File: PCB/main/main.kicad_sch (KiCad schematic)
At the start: 4 parts, among them J1 Conn_01x33_Female, J2 Conn_01x33_Female, J3 Conn_01x33_Female, J4 Conn_01x33_Female

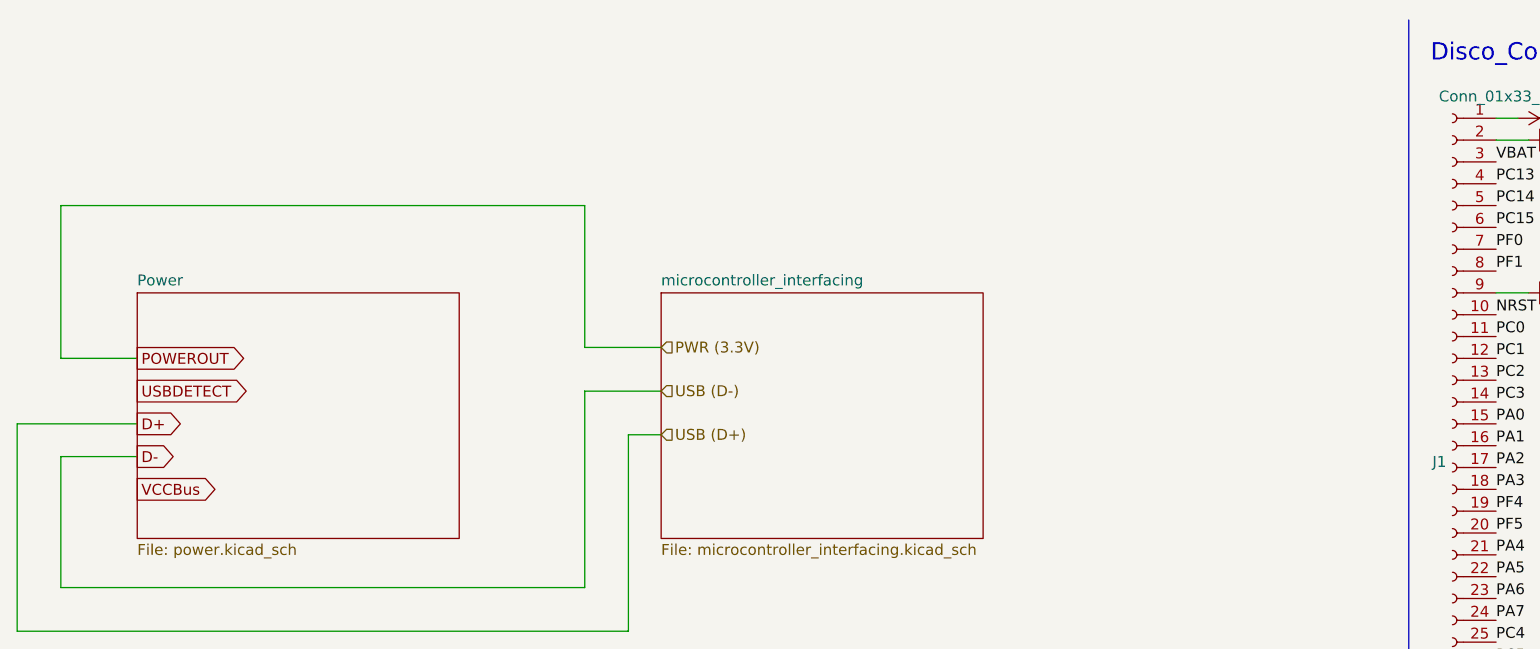
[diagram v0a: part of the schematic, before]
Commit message: Power v0.1, Sensing v0.1, uC Control v0.1, ERC
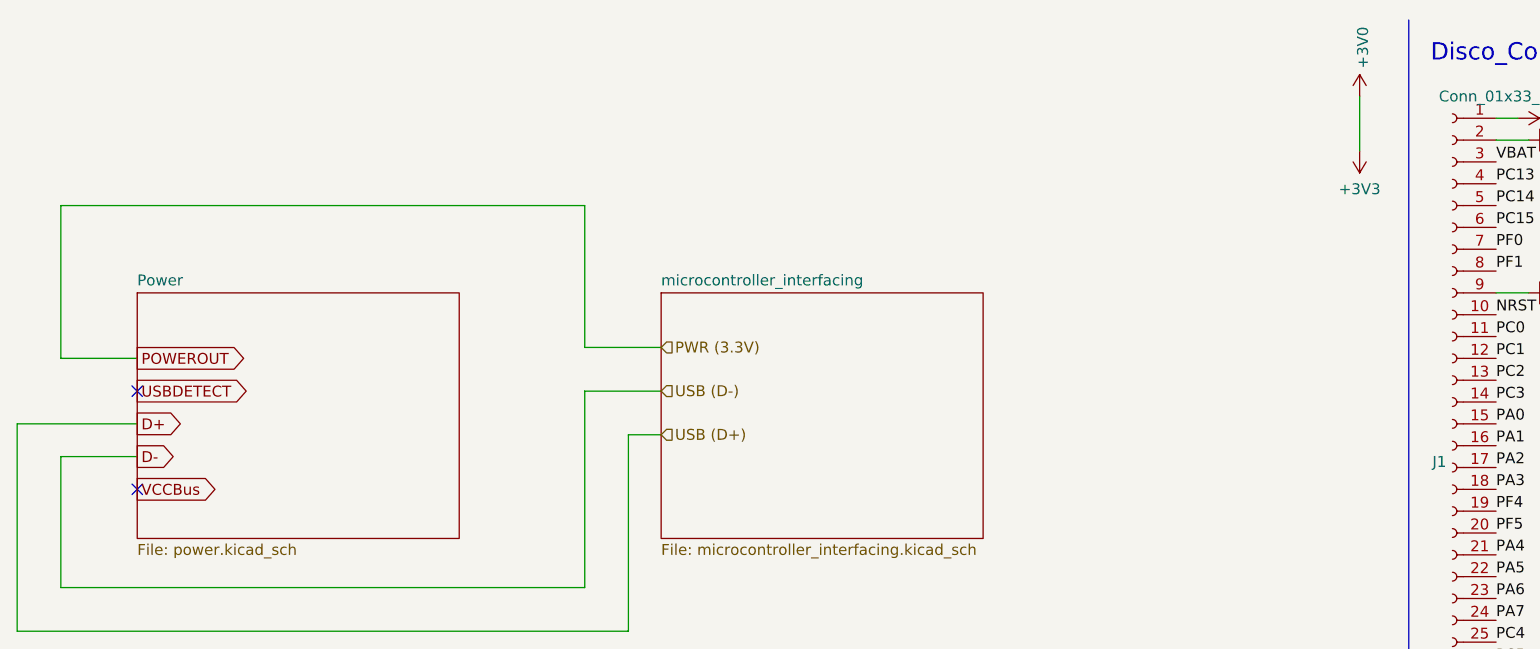
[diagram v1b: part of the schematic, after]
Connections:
- no-connect marks 0 -> 2

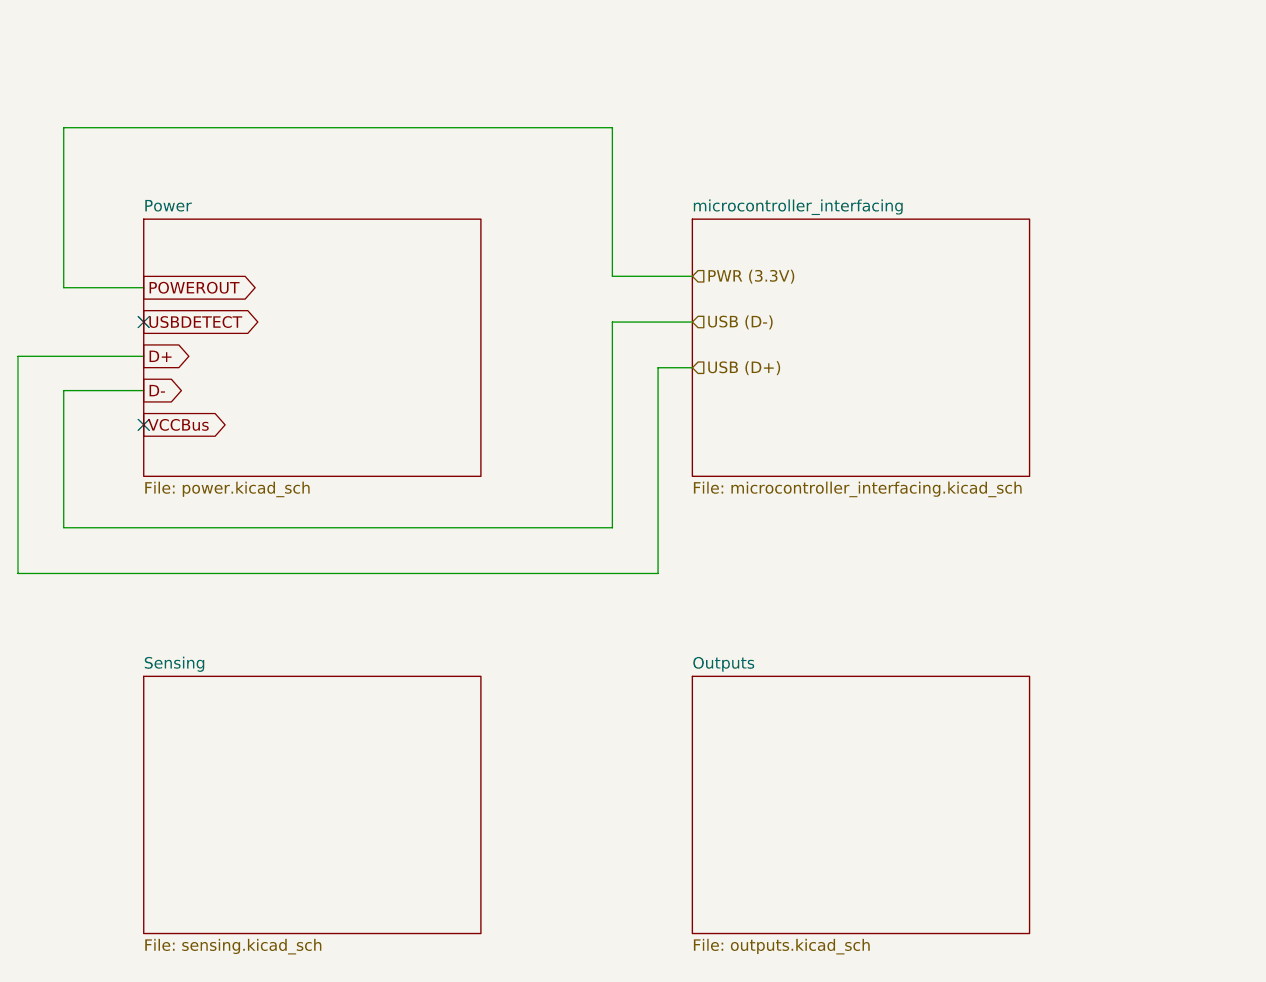
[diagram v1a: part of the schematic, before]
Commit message: Schematic updates
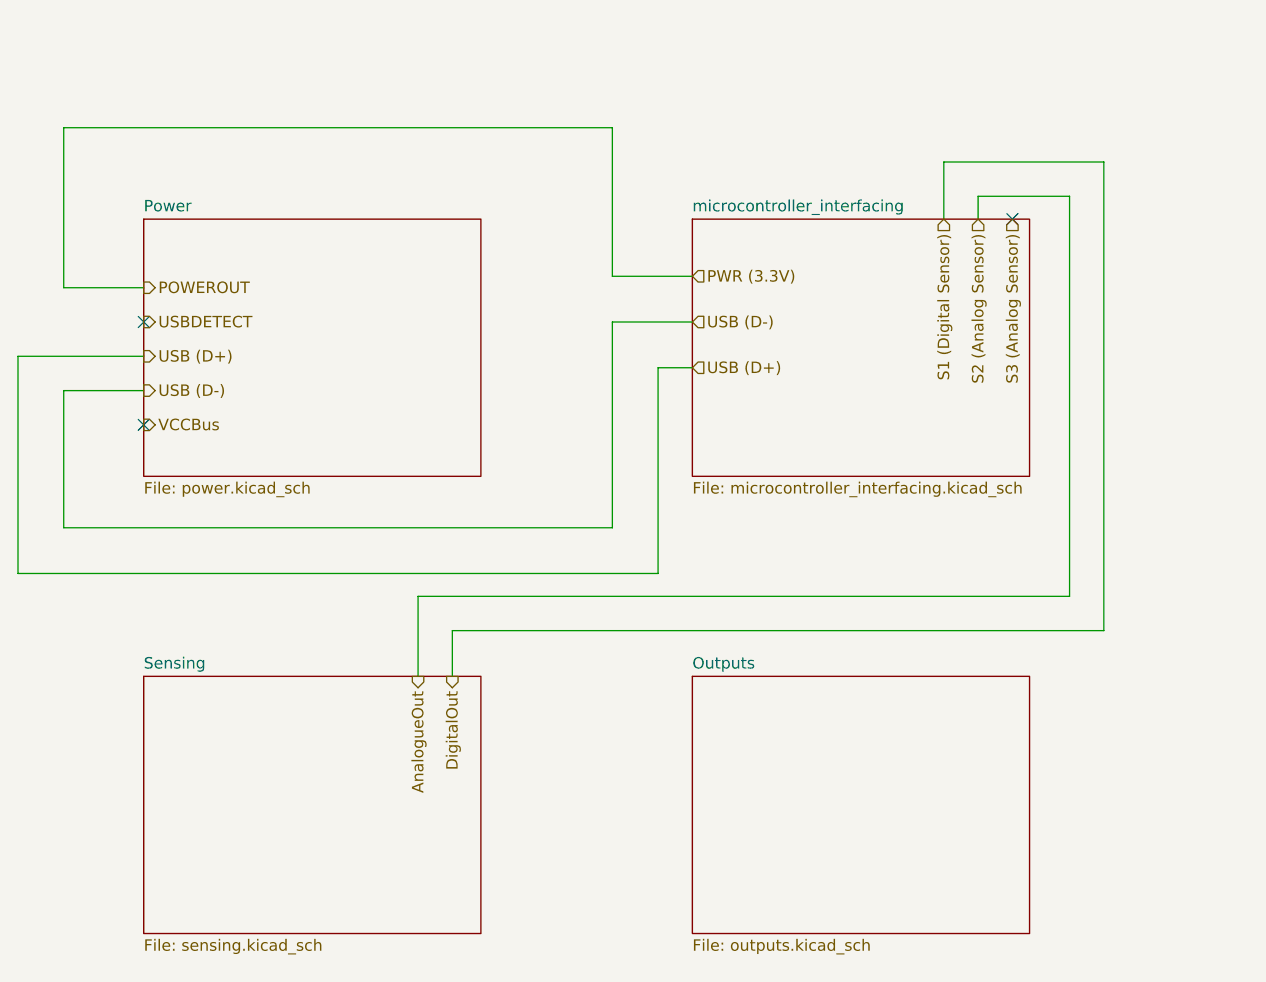
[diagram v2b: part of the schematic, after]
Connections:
- no-connect marks 2 -> 3

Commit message: Power, uC, Sensing v0.1.1
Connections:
- no-connect marks 3 -> 2
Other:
- sheet Power ports: added POWEROUT, USB (D+), USB (D-), USBDETECT, VCCBus; removed none
- sheet Sensing ports: added 3V3, AnalogueOut, DigitalOut; removed none
- sheet microcontroller_interfacing ports: added 3V3, PA1, PA10, PA2, PA3, PA9, PB6, PB7, S1 (Digital Sensor), S2 (Analog Sensor), USB (D+), USB (D-); removed none
